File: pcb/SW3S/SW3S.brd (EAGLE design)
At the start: 50 x 35.6 mm, 52 parts, among them K1 PROG, T1 BC807, T2 BC817, T4 IRL3303, T5 IRL3303

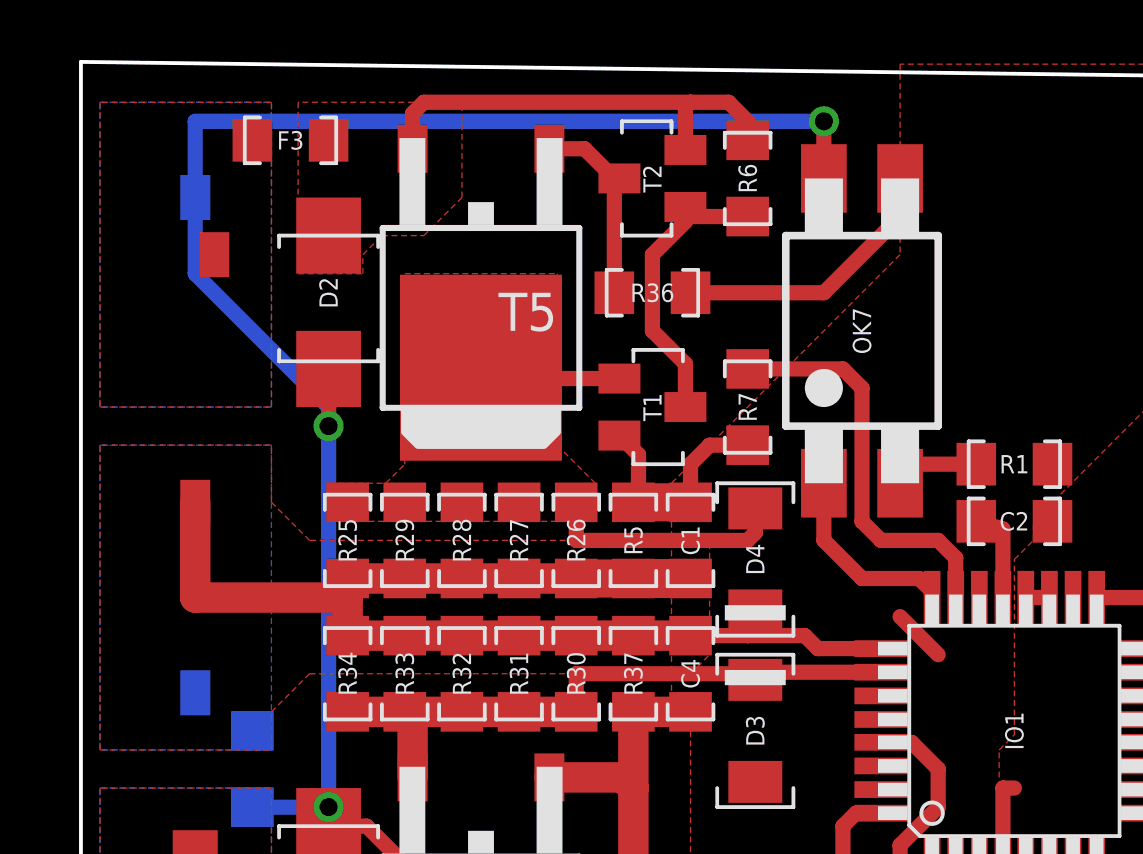
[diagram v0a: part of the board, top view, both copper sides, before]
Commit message: Regulace maximalniho nabijeciho proudu neni potreba
V prvni fazi se nabiji baterie konstantnim proudem a v pripade dosazeni U 4.15V/clanek (rezerva 50mV) se nabijeni uplne odpoji.
V pripade kdy balancer nebude stihat vyvazit baterii se tez nabijeni odpoji do okamziku vyvazeni vsech clanku baterie pod mez danou fw.
V pripade podvybiti baterie pod 3V elektronika nepovoli nabijeni (baterii je nutno nabit externi "inteligentni" nabijeckou.

Pozor:

Je potreba nabijet ze zdroje 12-14V kvuli ubytku napeti / ztratovem vykonu na regulacnim tranzistoru.
Ve firmware musi byt odpojeni nabijeni v pripade prehrati CPU nad stanovenou, docela nizkou mez !!! (CPU je blizko regulacniho T)
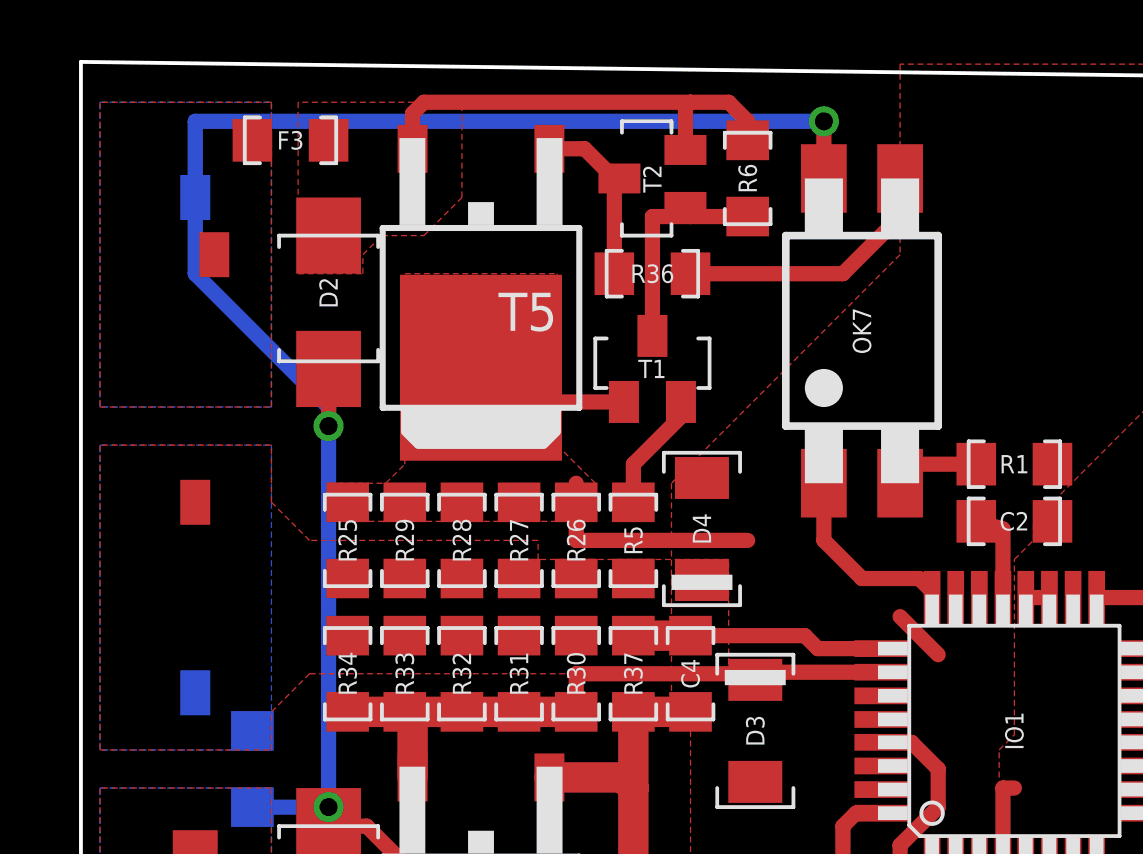
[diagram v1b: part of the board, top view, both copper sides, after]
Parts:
- removed C1: 100n, !discrete:0805
- removed R7: 400R, !discrete:0805
- R5: value 100R -> 0
- moved D4 2.05 mm to (20.7, 19.4)
- moved T1 1.27 mm to (19.1, 24.8), turned to 0 degrees
- moved R36 0.64 mm to (19.1, 27.9)
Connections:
- removed net N$5: IO1.23, R7.2
- removed net N$8: C1.2, R5.1, R7.1, T1.3
- new net N$21: R5.1, T1.3
- net BAT-: no longer C1.1
- net GND: now also IO1.23
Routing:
- net BAT-: track 42.4 -> 8.43 mm
- net N$5: track 13.5 -> 0.00 mm
- net N$8: track 8.35 -> 0.00 mm
- net N$21: track 0.00 -> 4.00 mm
- net GND: track 24.0 -> 21.6 mm
- net N$9: track 9.79 -> 7.52 mm
- net N$10: track 6.63 -> 5.99 mm
